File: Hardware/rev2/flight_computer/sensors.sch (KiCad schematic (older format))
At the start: 17 parts, among them U10 CAM-M8Q-0, U11 BMI088, U12 LIS3MDLTR, U13 Barometer

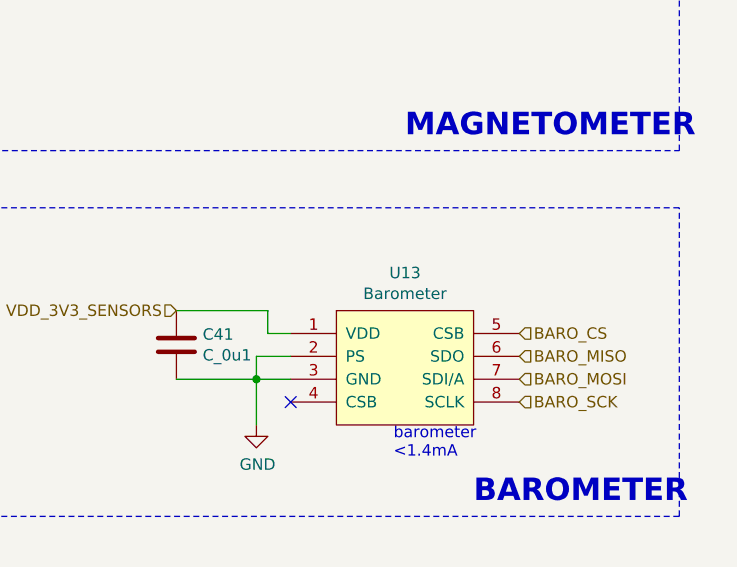
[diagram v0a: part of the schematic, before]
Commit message: Updates barometer part
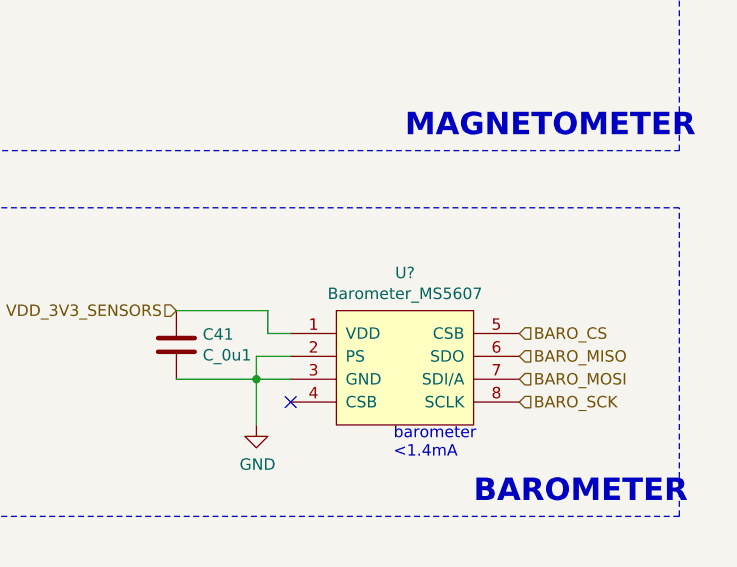
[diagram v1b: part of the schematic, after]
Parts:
- removed U13: Barometer, drone_footprints:MS561101BA03-50, symbol openDrone_parts:Barometer
- added U?: Barometer_MS5607, drone_footprints:MS561101BA03-50, symbol openDrone_parts:Barometer_MS5607
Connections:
- net BARO_CS: now also U?.5 (CSB)
- net BARO_MISO: now also U?.6 (SDO)
- net BARO_MOSI: now also U?.7 (SDI/A)
- net BARO_SCK: now also U?.8 (SCLK)
- net GND: now also U?.2 (PS), U?.3 (GND)
- net VDD_3V3_SENSORS: now also U?.1 (VDD)
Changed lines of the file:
@@
 	7400 1250 8000 1250
 Connection ~ 7400 1350
-$Comp
-L openDrone_parts:Barometer U13
-U 1 1 5F94F59C
-P 9450 3900
-F 0 "U13" H 9550 4165 50  0000 C CNN
-F 1 "Barometer" H 9550 4074 50  0000 C CNN
-F 2 "drone_footprints:MS561101BA03-50" H 9850 4250 50  0001 C CNN
-F 3 "" H 9850 4250 50  0001 C CNN
-F 4 "223-1622-1-ND" H 9550 4350 50  0001 C CNN "DPN"
-F 5 "MS561101BA03-50" H 9500 4250 50  0001 C CNN "MPN"
-	1    9450 3900
-	1    0    0    -1
-$EndComp
 Text HLabel 10050 3900 2    50   Input ~ 0
 BARO_CS
@@
 NoConn ~ 1850 1900
 NoConn ~ 9050 4200
+$Comp
+L openDrone_parts:Barometer_MS5607 U?
+U 1 1 600B9BDB
+P 9450 3900
+F 0 "U?" H 9550 4165 50  0000 C CNN
+F 1 "Barometer_MS5607" H 9550 4074 50  0000 C CNN
+F 2 "drone_footprints:MS561101BA03-50" H 9850 4250 50  0001 C CNN
+F 3 "https://www.te.com/commerce/DocumentDelivery/DDEController?Action=srchrtrv&DocNm=MS5607-02BA03&DocType=Data+Sheet&DocLang=English" H 9850 4250 50  0001 C CNN
+F 4 "223-1198-1-ND" H 9550 4350 50  0001 C CNN "DPN"
+F 5 " MS560702BA03-50 " H 9500 4250 50  0001 C CNN "MPN"
+	1    9450 3900
+	1    0    0    -1
+$EndComp
 $EndSCHEMATC
